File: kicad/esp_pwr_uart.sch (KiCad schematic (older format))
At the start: 32 parts, among them P1 USB_micro, Q1 DDC114TU, U131 1117-33, U132 CP2102N-A01-GQFN28

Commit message: replaced microUSB, Switches, Batt Holder, Capacitor per seeed suggestions
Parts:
- P1: footprint ClockIOT_libs:USB_Micro-B_Molex-105017-0001 -> ClockIOT_libs:USB_Micro-B_seeed-320010561
- S3, S4: footprint ClockIOT_libs:SW_SMD -> ClockIOT_libs:SW_SMD_311020004
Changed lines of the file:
@@
 F 0 "P1" H 1527 4148 40  0000 C CNB
 F 1 "USB_micro" H 1527 4073 40  0000 C CNB
-F 2 "ClockIOT_libs:USB_Micro-B_Molex-105017-0001" H 1475 4000 60  0001 C CNN
+F 2 "ClockIOT_libs:USB_Micro-B_seeed-320010561" H 1475 4000 60  0001 C CNN
 F 3 "" H 1475 4050 60  0000 C CNN
 	1    1475 4000
@@
 F 0 "S3" V 9525 1975 40  0000 C CNB
 F 1 "SW-EN" V 9625 2050 40  0000 C CNB
-F 2 "ClockIOT_libs:SW_SMD" H 9575 1750 60  0001 C CNN
+F 2 "ClockIOT_libs:SW_SMD_311020004" H 9575 1750 60  0001 C CNN
 F 3 "" H 9575 1750 60  0000 C CNN
 F 4 "Value" H 9575 1750 50  0001 C CNN "manf#"
@@
 F 0 "S4" V 9525 3375 40  0000 C CNB
 F 1 "SW-BOOT" V 9650 3475 40  0000 C CNB
-F 2 "ClockIOT_libs:SW_SMD" H 9575 3150 60  0001 C CNN
+F 2 "ClockIOT_libs:SW_SMD_311020004" H 9575 3150 60  0001 C CNN
 F 3 "" H 9575 3150 60  0000 C CNN
 F 4 "Value" H 9575 3150 50  0001 C CNN "manf#"

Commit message: cleanup
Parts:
- D1: value RClamp0854P.TCT -> PRTR5V0U2X
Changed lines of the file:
@@
 P 2275 5100
 F 0 "D1" H 2500 5000 50  0000 L CNN
-F 1 "RClamp0854P.TCT" H 2200 4900 50  0000 L CNN
+F 1 "PRTR5V0U2X" H 2200 4900 50  0000 L CNN
 F 2 "ClockIOT_libs:SOT-143" H 2275 5100 50  0001 C CNN
 F 3 "" H 2275 5100 50  0001 C CNN

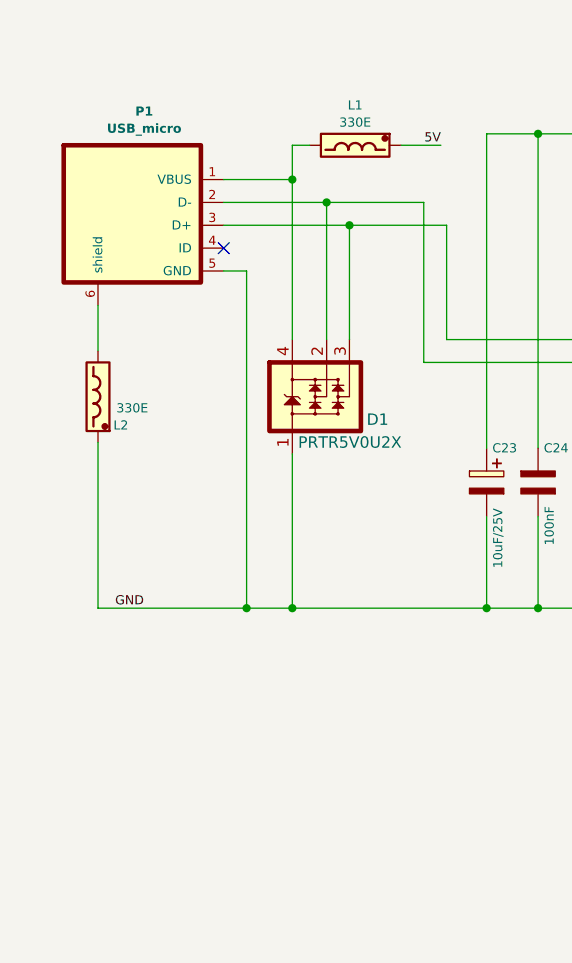
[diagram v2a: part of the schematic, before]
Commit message: added USB-C breakout footprint to PCB
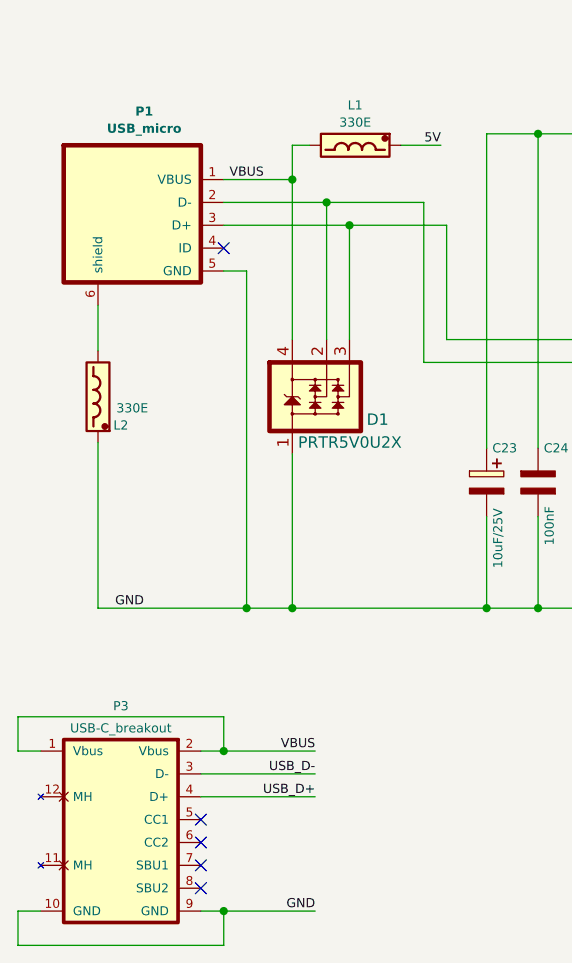
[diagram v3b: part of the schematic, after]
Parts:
- added P3: USB-C_breakout, ClockIOT_libs:USB-C_bout, symbol ClockIOT:USB-C_breakout
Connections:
- net GND: now also P3.10 (GND), P3.9 (GND)
- net USB_D+: now also P3.4 (D+)
- net USB_D-: now also P3.3 (D-)
- net VBUS: now reaches D1.4, L1.2, P1.1 (VBUS)
- net VBUS: now also P3.1 (Vbus), P3.2 (Vbus)
- no-connect marks 7 -> 11
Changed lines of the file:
@@
 Wire Wire Line
 	1325 5300 1325 6025
+$Comp
+L ClockIOT:USB-C_breakout P3
+U 1 1 5BCA34C2
+P 1425 7000
+F 0 "P3" H 1425 7547 40  0000 C CNN
+F 1 "USB-C_breakout" H 1425 7450 40  0000 C CNN
+F 2 "ClockIOT_libs:USB-C_bout" H 1675 7150 40  0001 C CNN
+F 3 "" H 1675 7150 40  0001 C CNN
+	1    1425 7000
+	1    0    0    -1
+$EndComp
+NoConn ~ 1775 6950
+NoConn ~ 1775 7050
+NoConn ~ 1775 7150
+NoConn ~ 1775 7250
+Text Label 2275 6750 2    40   ~ 0
+USB_D-
+Text Label 2275 6850 2    40   ~ 0
+USB_D+
+Text Label 2275 7350 2    40   ~ 0
+GND
+Wire Wire Line
+	1075 7350 975  7350
+Wire Wire Line
+	975  7350 975  7500
+Wire Wire Line
+	975  7500 1875 7500
+Wire Wire Line
+	1875 7500 1875 7350
+Wire Wire Line
+	1775 7350 1875 7350
+Wire Wire Line
+	1875 7350 2275 7350
+Connection ~ 1875 7350
+Wire Wire Line
+	2275 6750 1775 6750
+Wire Wire Line
+	2275 6850 1775 6850
+Wire Wire Line
+	1075 6650 975  6650
+Wire Wire Line
+	975  6650 975  6500
+Wire Wire Line
+	975  6500 1875 6500
+Wire Wire Line
+	1875 6500 1875 6650
+Wire Wire Line
+	1875 6650 1775 6650
+Text Label 1900 4150 0    40   ~ 0
+VBUS
+Text Label 2275 6650 2    40   ~ 0
+VBUS
+Wire Wire Line
+	2275 6650 1875 6650
+Connection ~ 1875 6650
 $EndSCHEMATC

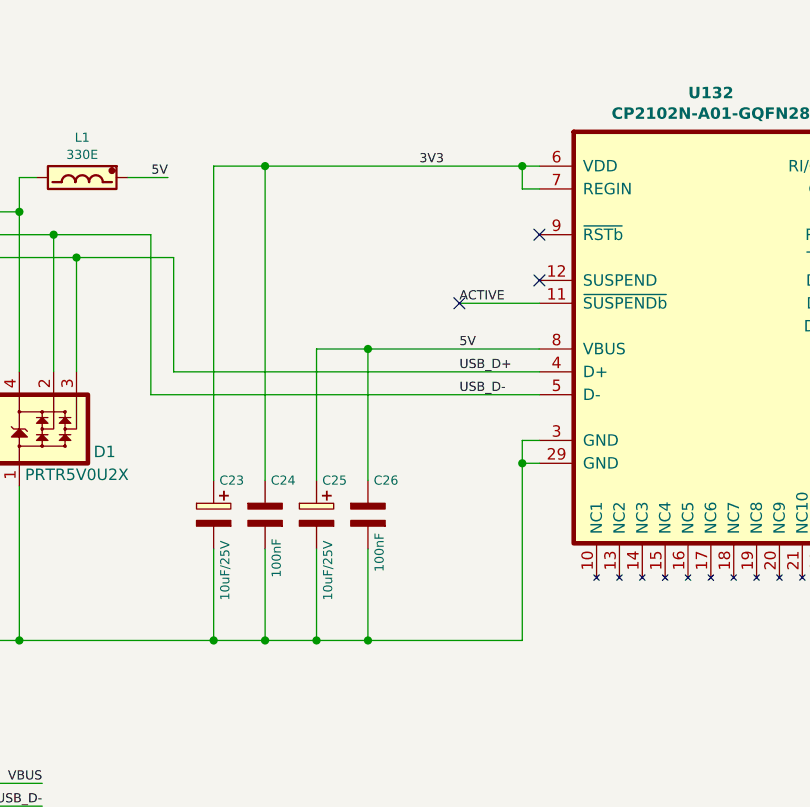
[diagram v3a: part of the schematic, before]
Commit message: added pullup for RST and pulldown for SUSPEND CP2102
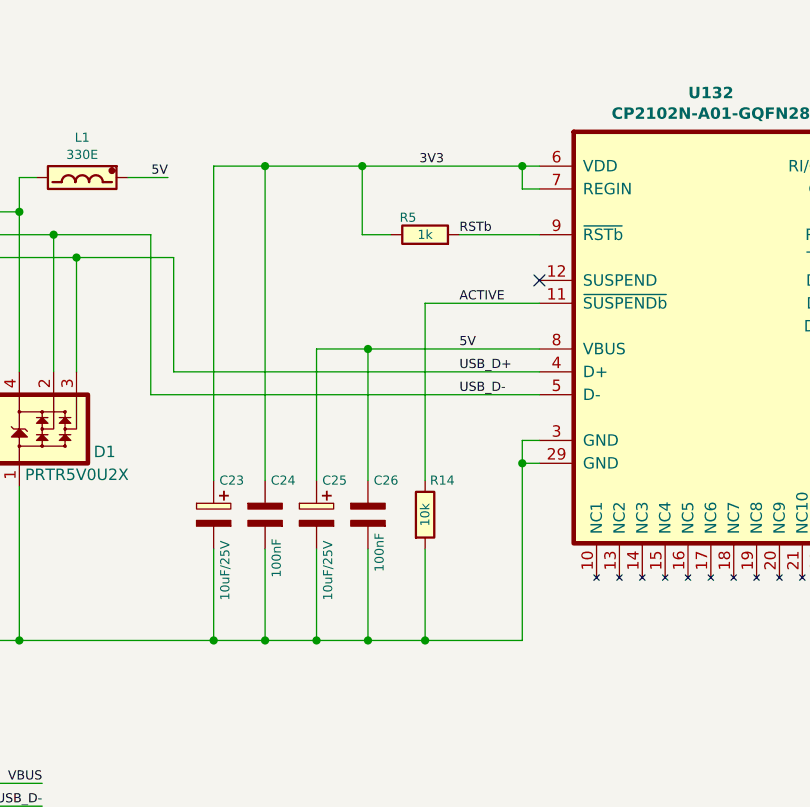
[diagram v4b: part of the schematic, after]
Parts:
- added R14: 10k, ClockIOT_libs:r_0805, symbol ClockIOT:R
- added R5: 1k, ClockIOT_libs:r_0805, symbol ClockIOT:R
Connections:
- net 3V3: now also R5.1
- net ACTIVE: now also R14.1
- net GND: now also R14.2
- net RSTb: now reaches U132.9 (~RSTb)
- net RSTb: now also R5.2
- no-connect marks 11 -> 9
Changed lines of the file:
@@
 	1975 4550 1975 6025
 Wire Wire Line
-	4375 6025 3700 6025
+	4375 6025 3950 6025
 Wire Wire Line
 	4375 5250 4450 5250
@@
 	3700 4750 3700 5325
 Connection ~ 3700 4750
-NoConn ~ 4450 4250
-Wire Wire Line
-	4450 4550 4100 4550
 NoConn ~ 4450 4450
 Text Label 4100 4550 0    40   ~ 0
@@
 	2775 2575 2775 2475
 Connection ~ 2625 2575
-NoConn ~ 4100 4550
 NoConn ~ 7400 4650
 NoConn ~ 7400 4450
@@
 	3700 6025 3475 6025
 Wire Wire Line
-	3250 3950 4375 3950
+	3250 3950 3675 3950
 Wire Wire Line
 	3700 4750 4450 4750
@@
 	2275 6650 1875 6650
 Connection ~ 1875 6650
+$Comp
+L ClockIOT:R R5
+U 1 1 5BCE1E3D
+P 3950 4250
+F 0 "R5" V 4025 4325 40  0000 C CNN
+F 1 "1k" V 3950 4250 40  0000 C CNN
+F 2 "ClockIOT_libs:r_0805" V 3880 4250 30  0001 C CNN
+F 3 "" H 3950 4250 30  0000 C CNN
+F 4 "Value" H 3950 4250 50  0001 C CNN "manf#"
+	1    3950 4250
+	0    -1   -1   0
+$EndComp
+Wire Wire Line
+	4450 4250 4100 4250
+Wire Wire Line
+	3800 4250 3675 4250
+Wire Wire Line
+	3675 4250 3675 3950
+Connection ~ 3675 3950
+Wire Wire Line
+	3675 3950 4375 3950
+$Comp
+L ClockIOT:R R14
+U 1 1 5BCEFFA9
+P 3950 5475
+F 0 "R14" H 4025 5625 40  0000 C CNN
+F 1 "10k" V 3950 5475 40  0000 C CNN
+F 2 "ClockIOT_libs:r_0805" V 3880 5475 30  0001 C CNN
+F 3 "" H 3950 5475 30  0000 C CNN
+F 4 "Value" H 3950 5475 50  0001 C CNN "manf#"
+	1    3950 5475
+	1    0    0    -1
+$EndComp
+Wire Wire Line
+	3950 5625 3950 6025
+Connection ~ 3950 6025
+Wire Wire Line
+	3950 6025 3700 6025
+Wire Wire Line
+	3950 5325 3950 4550
+Wire Wire Line
+	3950 4550 4450 4550
+Text Label 4100 4250 0    40   ~ 0
+RSTb
 $EndSCHEMATC
